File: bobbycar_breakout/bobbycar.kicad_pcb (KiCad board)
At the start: 2 copper layers, 61.7 x 26.9 mm, 29 parts, among them J1 Conn_01x04, J2 Conn_01x04, J3 Screw_Terminal_01x02, J4 Screw_Terminal_01x02, J5 Screw_Terminal_01x02, J6 Conn_01x04, U1 L7805SOT89

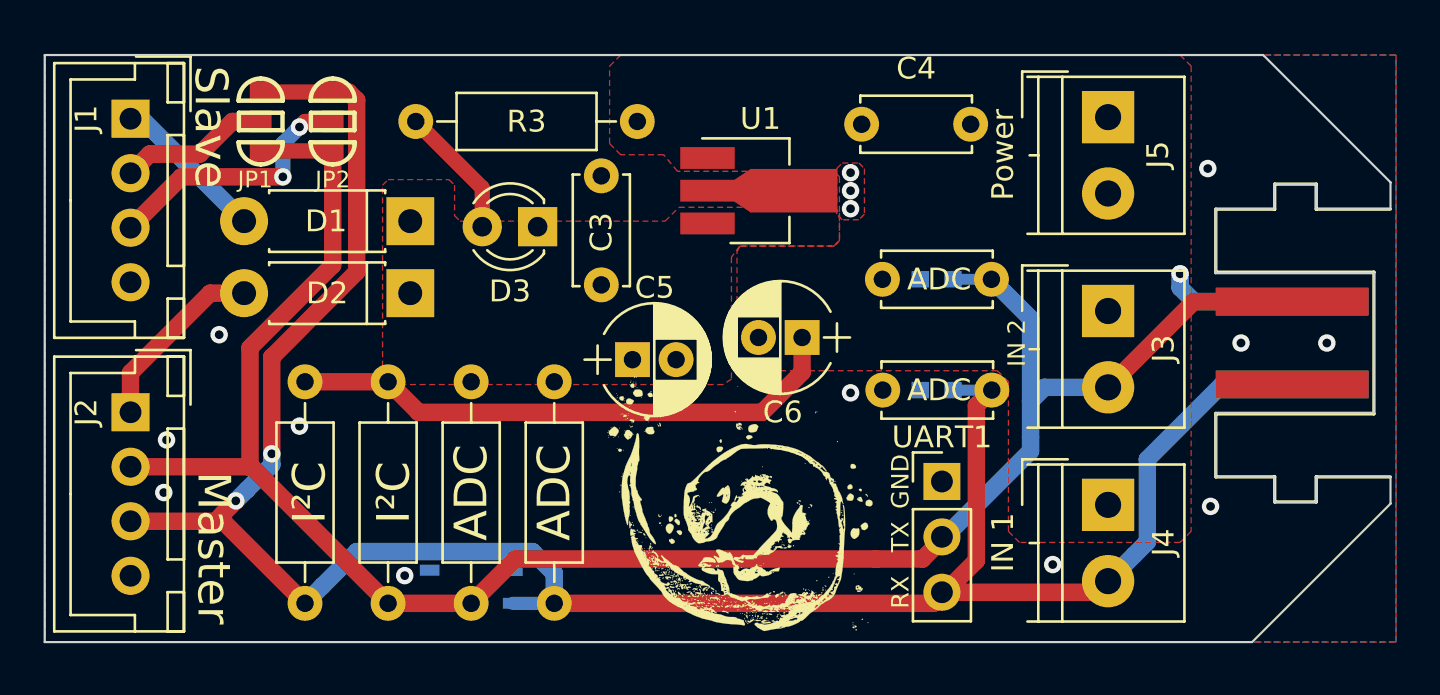
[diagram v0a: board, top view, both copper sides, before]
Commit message: updated to kicad 6
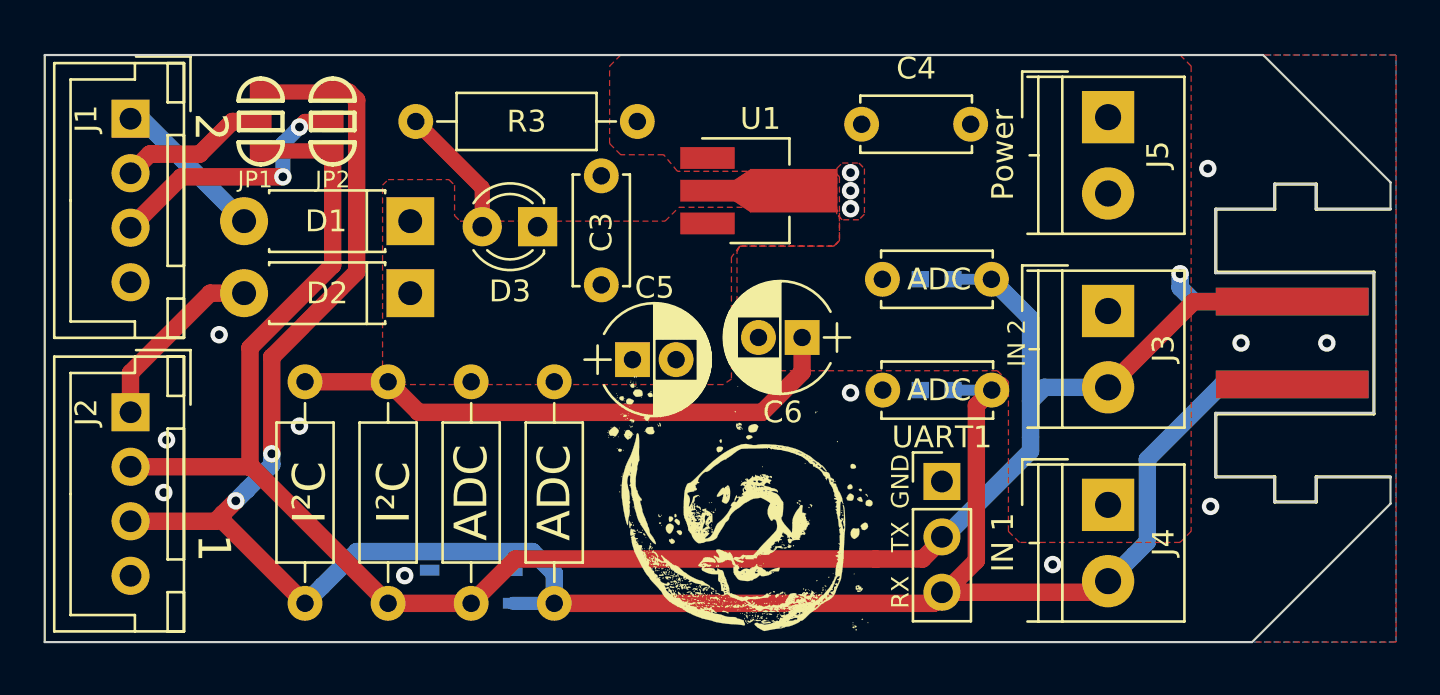
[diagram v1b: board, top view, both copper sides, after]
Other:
- net class Default removed
- board text added: "1"
- board text added: "2"
- board text added: "Lucy Fauth, Jana Marie Hemsing"
- board text removed: "Master"
- board text removed: "Niklas Fauth, Jan Henrik Hemsing"
- board text removed: "Slave"
